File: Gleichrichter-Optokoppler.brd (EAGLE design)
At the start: 44.4 x 36.5 mm, 9 parts, among them X2 22-23-2041

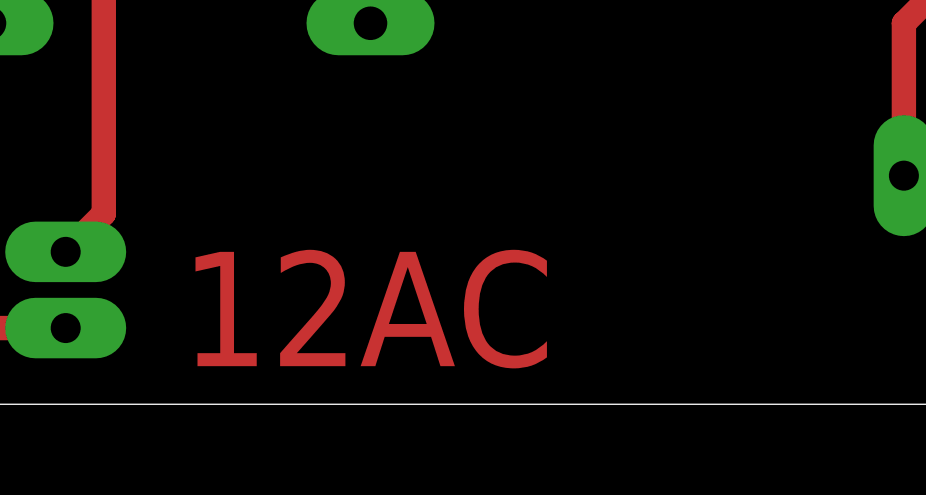
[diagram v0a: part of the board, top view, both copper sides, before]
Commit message: datasheet of 4N38A and powersupply text
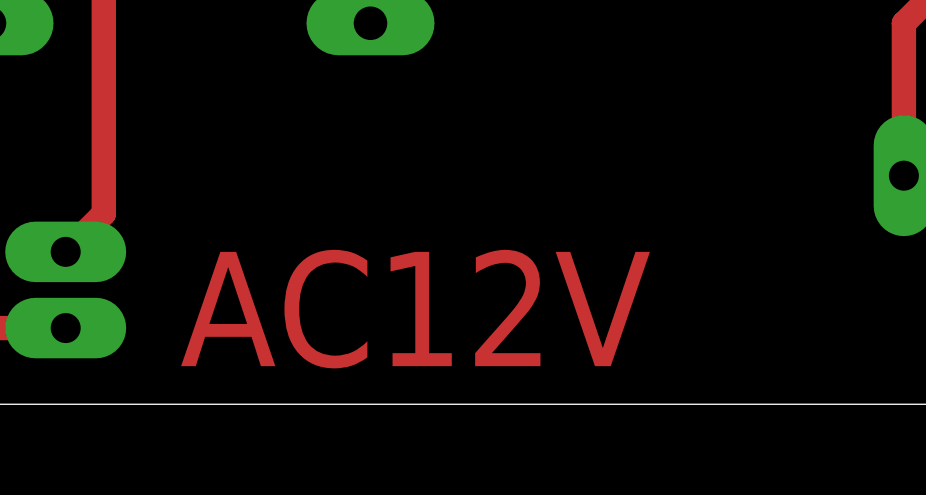
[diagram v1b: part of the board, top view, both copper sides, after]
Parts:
- R1: value 1k -> 1.5k
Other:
- board text added: "AC12V"
- board text removed: "12AC"
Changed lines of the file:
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@@
 <layer number="35" name="tGlue" color="7" fill="4" visible="no" active="yes"/>
 <layer number="36" name="bGlue" color="7" fill="5" visible="no" active="yes"/>
-<layer number="37" name="tTest" color="7" fill="1" visible="no" active="yes"/>
-<layer number="38" name="bTest" color="7" fill="1" visible="no" active="yes"/>
+<layer number="37" name="tTest" color="7" fill="1" visible="yes" active="yes"/>
+<layer number="38" name="bTest" color="7" fill="1" visible="yes" active="yes"/>
 <layer number="39" name="tKeepout" color="4" fill="11" visible="yes" active="yes"/>
 <layer number="40" name="bKeepout" color="1" fill="11" visible="yes" active="yes"/>
@@
 <layer number="42" name="bRestrict" color="1" fill="10" visible="yes" active="yes"/>
 <layer number="43" name="vRestrict" color="2" fill="10" visible="yes" active="yes"/>
-<layer number="44" name="Drills" color="7" fill="1" visible="no" active="yes"/>
+<layer number="44" name="Drills" color="7" fill="1" visible="yes" active="yes"/>
 <layer number="45" name="Holes" color="7" fill="1" visible="yes" active="yes"/>
-<layer number="46" name="Milling" color="3" fill="1" visible="no" active="yes"/>
-<layer number="47" name="Measures" color="7" fill="1" visible="no" active="yes"/>
+<layer number="46" name="Milling" color="3" fill="1" visible="yes" active="yes"/>
+<layer number="47" name="Measures" color="7" fill="1" visible="yes" active="yes"/>
 <layer number="48" name="Document" color="7" fill="1" visible="yes" active="yes"/>
 <layer number="49" name="Reference" color="7" fill="1" visible="yes" active="yes"/>
@@
 <wire x1="0" y1="36.5" x2="0" y2="0" width="0" layer="20"/>
 <text x="6.35" y="30.48" size="5.08" layer="1" font="vector" distance="0">ver 0.2</text>
-<text x="10.16" y="1.27" size="3.81" layer="1" font="vector" distance="0">12AC</text>
+<text x="10.16" y="1.27" size="3.81" layer="1" font="vector" distance="0">AC12V</text>
 <hole x="41.91" y="33.02" drill="0.6"/>
 <hole x="41.91" y="2.54" drill="0.6"/>
@@
 </autorouter>
 <elements>
-<element name="R1" library="eagle-ltspice" package="0207/10" value="1k" x="30.48" y="27.94" rot="MR180">
+<element name="R1" library="eagle-ltspice" package="0207/10" value="1.5k" x="30.48" y="27.94" rot="MR180">
 <attribute name="SPICEMODEL" value="NONE" x="67.31" y="63.5" size="1.778" layer="28" rot="MR180" display="off"/>
 <attribute name="SPICEPREFIX" value="R" x="67.31" y="63.5" size="1.778" layer="28" rot="MR180" display="off"/>
